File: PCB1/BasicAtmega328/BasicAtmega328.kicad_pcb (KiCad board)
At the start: 2 copper layers, 0 parts

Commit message: Placa enrutada
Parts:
- added C1: 47uF, Capacitors_SMD:CP_Elec_6.3x5.7, F.Cu at (110.5, 97.8)
- added C2: 100nF, Capacitors_SMD:C_0805, F.Cu at (104.1, 78.7)
- added C3: 4.7uF, Capacitors_SMD:C_0805, F.Cu at (102.5, 77.1)
- added C5: 100nF, Capacitors_SMD:C_0805, F.Cu at (113.6, 89.5)
- added C6: 100nF, Capacitors_SMD:C_0805, F.Cu at (97.3, 97.6)
- added C7: 10uF, Capacitors_SMD:C_0805, F.Cu at (118.8, 82.0)
- added C8: 100nF, Capacitors_SMD:C_0805, F.Cu at (118.8, 80.1)
- added D1: MBRA140, Diodes_SMD:D_SMA_Standard, F.Cu at (121.5, 93.0)
- added D2: POWER_ON, LEDs:LED_0805, B.Cu at (113.0, 105.4)
- added D3: SMBJ6.0CA, Diode_SMD:D_SMB, B.Cu at (117.4, 71.3)
- added D4: SMBJ6.0CA, Diode_SMD:D_SMB, B.Cu at (109.1, 71.3)
- added D5: SMBJ6.0CA, Diode_SMD:D_SMB, B.Cu at (100.8, 71.3)
- added F1: 160mA, Fuses:1206, B.Cu at (123.4, 66.4)
- added F2: 160mA, Fuses:1206, B.Cu at (94.7, 66.3)
- added J1: Jack-DC-IN, Connectors:BARREL_JACK, F.Cu at (118.8, 97.0)
- added JP1: VCC_CUT, Jumpers:SMT-JUMPER_2_NO_NO-SILK, B.Cu at (97.5, 84.7)
- added JP2: VCC_CUT, Jumpers:SMT-JUMPER_2_NO_NO-SILK, B.Cu at (119.1, 80.4)
- added JP3: VCC_CUT, Jumpers:SMT-JUMPER_2_NO_NO-SILK, B.Cu at (100.6, 104.3)
- added P1: ISCP, Connectors:2X3, F.Cu at (94.9, 89.3)
- added P2: HEADER1, Pin_Headers:Pin_Header_Straight_1x15, F.Cu at (88.4, 64.2)
- added P3: MODBUS_1, Connectors_Molex:Molex_Microfit3_Header_02x03_Angled_43045-060x, F.Cu at (113.7, 63.4)
- added P4: SERIAL_DEBUG, Connectors_JST:JST_PH_S4B-PH-K_04x2.00mm_Angled, F.Cu at (102.5, 105.0)
- added P5: MODBUS_2, Connectors_Molex:Molex_Microfit3_Header_02x03_Angled_43045-060x, F.Cu at (97.9, 63.4)
- added P6: HEADER2, Pin_Headers:Pin_Header_Straight_1x15, F.Cu at (129.4, 64.4)
- added R1: 1k, Resistors_SMD:R_0805, B.Cu at (113.0, 103.5)
- added R2: 10k, Resistors_SMD:R_0805, F.Cu at (108.1, 74.0)
- added R3: 10k, Resistors_SMD:R_0805, F.Cu at (108.1, 75.9)
- added R4: 1k, Resistors_SMD:R_0805, F.Cu at (98.6, 104.6)
- added R5: 10k, Resistors_SMD:R_0805, F.Cu at (124.1, 73.9)
- added R6: 10k, Resistors_SMD:R_0805, F.Cu at (122.2, 69.8)
- added R7: 10k, Resistors_SMD:R_0805, F.Cu at (111.7, 75.4)
- added R8: 120R(NC), Resistors_SMD:R_0805, B.Cu at (115.3, 73.8)
- added SW1: RESET_Button, Buttons_Switches_SMD:SW_SPST_B3U-3000P, F.Cu at (95.0, 105.1)
- added U1: LM1117-5.0, TO_SOT_Packages_SMD:SOT-223-3_TabPin2, F.Cu at (102.6, 97.9)
- added U2: ATMEGA328P-AU, Housings_QFP:TQFP-32_7x7mm_Pitch0.8mm, F.Cu at (108.1, 84.8)
- added U3: MAX13487E, Housings_SOIC:SO-8_5.3x6.2mm_Pitch1.27mm, F.Cu at (117.9, 75.7)
- added Y1: 16Mhz, Clocks:RESONATOR-SMD-3.2X1.3, F.Cu at (101.2, 81.5)
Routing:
- net +5V: track 0.00 -> 131.6 mm, vias 0 -> 5
- net +12V: track 0.00 -> 102.0 mm, vias 0 -> 3
- net RST: track 0.00 -> 95.8 mm, vias 0 -> 5
- net TXD: track 0.00 -> 59.0 mm, vias 0 -> 2
- net RXD: track 0.00 -> 58.1 mm, vias 0 -> 3
- net 485_TX: track 0.00 -> 49.6 mm, vias 0 -> 3
- net D13-SCK: track 0.00 -> 49.0 mm, vias 0 -> 7
- net 485_RX: track 0.00 -> 41.1 mm, vias 0 -> 2
- net Net-(D4-Pad2): track 0.00 -> 32.3 mm, vias 0 -> 2
- net D12-MISO: track 0.00 -> 31.0 mm
- net D11-MOSI: track 0.00 -> 29.5 mm, vias 0 -> 1
- net Net-(D3-Pad2): track 0.00 -> 28.6 mm, vias 0 -> 3
- net A6: track 0.00 -> 26.0 mm, vias 0 -> 2
- net A7: track 0.00 -> 25.4 mm, vias 0 -> 2
- net D10: track 0.00 -> 25.0 mm
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- added copper zone on B.Cu, net GND
- added copper zone on F.Cu, net GND
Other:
- board outline added: 45 x 49.9 mm

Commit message: Serigrafia añadida, faltan logos y DRC
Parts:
- added REF**: MountingHole_3.2mm_M3, Mounting_Holes:MountingHole_3.2mm_M3, F.Cu at (87.9, 106.6)
- added REF**: MountingHole_3.2mm_M3, Mounting_Holes:MountingHole_3.2mm_M3, F.Cu at (129.8, 106.7)
- added REF**: MountingHole_3.2mm_M3, Mounting_Holes:MountingHole_3.2mm_M3, F.Cu at (129.8, 58.5)
- added REF**: MountingHole_3.2mm_M3, Mounting_Holes:MountingHole_3.2mm_M3, F.Cu at (87.9, 58.4)
- moved D2 3.86 mm to (112.0, 109.1)
- moved R1 3.86 mm to (112.1, 107.2)
- moved SW1 3.55 mm to (96.2, 108.4)
- moved JP3 3.08 mm to (97.6, 103.3)
- moved R4 2.39 mm to (96.4, 105.5), turned to 180 degrees
- moved R8 2.21 mm to (117.3, 74.9)
- moved P4 1.15 mm to (101.4, 104.9)
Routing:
- net +5V: track 131.6 -> 142.3 mm
- net GND: track 9.15 -> 13.9 mm, vias 55 -> 88
- net RST: track 95.8 -> 99.5 mm
- net RXD: track 58.1 -> 61.1 mm
- net Net-(D3-Pad2): track 28.6 -> 31.1 mm
- net Net-(JP3-Pad2): track 3.04 -> 5.19 mm
- net Net-(D4-Pad2): track 32.3 -> 30.6 mm
- net A2: track 17.8 -> 18.5 mm
- net D6: track 17.6 -> 17.0 mm
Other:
- board size 45 x 49.9 mm -> 48.8 x 55.1 mm
- board text added: "BasicAtmega V0.1"

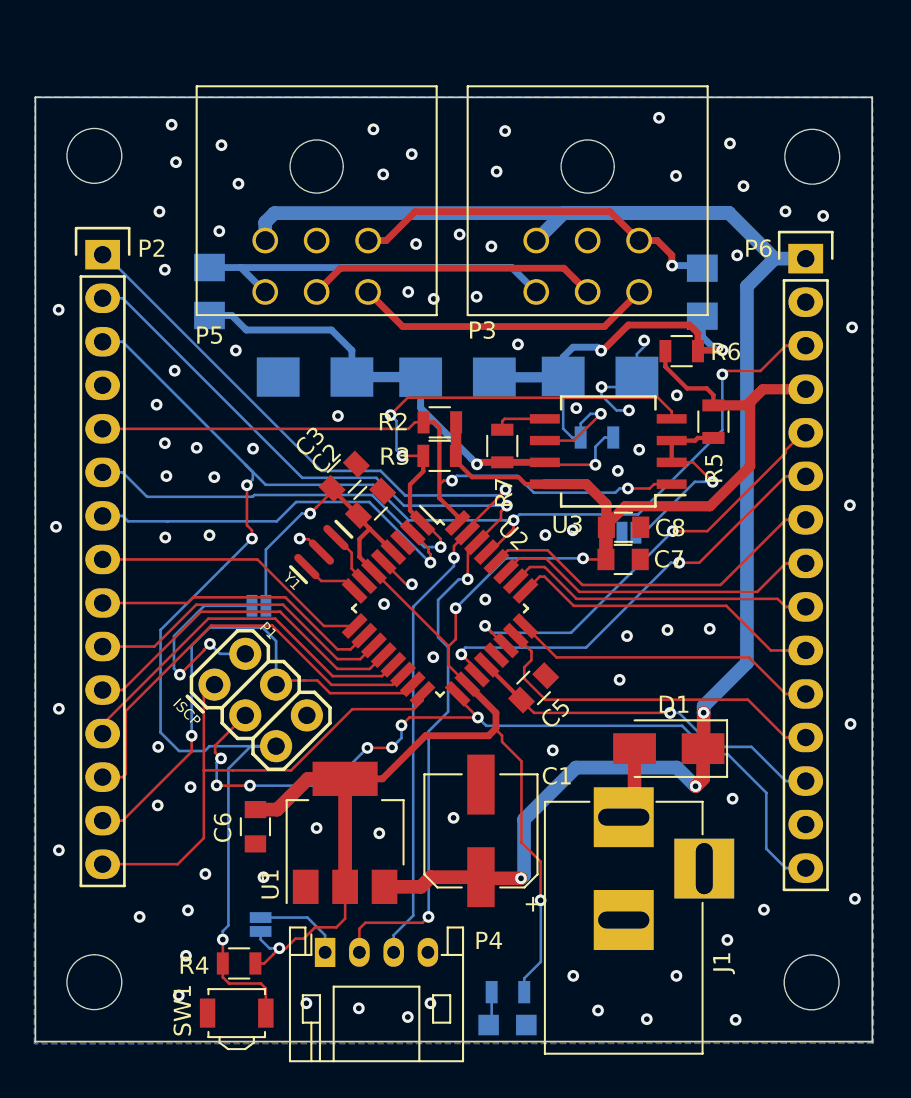
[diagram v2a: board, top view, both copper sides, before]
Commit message: Placas deconexion terminadas
Medidas exactas, esquema de drivers avanzado
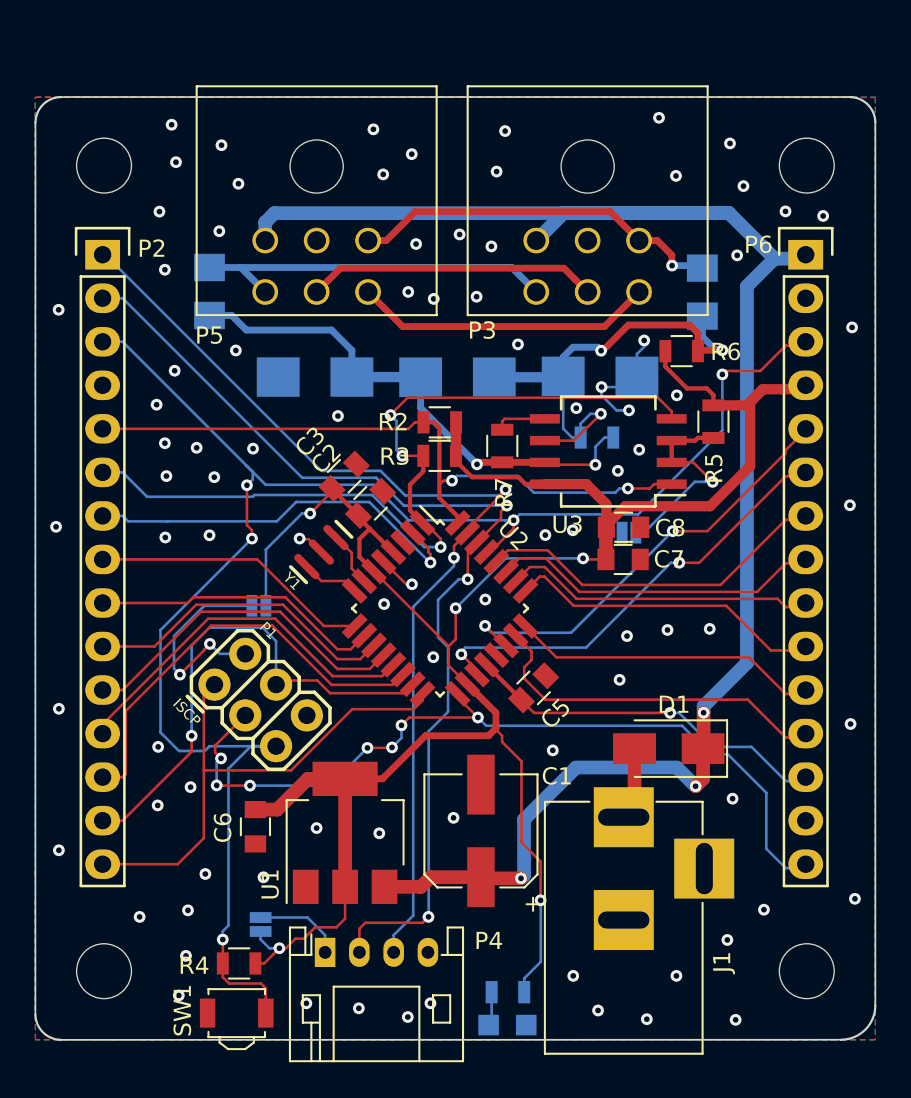
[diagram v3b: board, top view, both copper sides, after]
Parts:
- moved REF** 0.86 mm to (88.5, 106.0)
- moved REF** 0.80 mm to (88.5, 59.0)
- moved REF** 0.71 mm to (129.5, 106.0)
- moved REF** 0.61 mm to (129.5, 59.0)
- moved P6 0.23 mm to (129.4, 64.2)
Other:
- board size 48.8 x 55.1 mm -> 49 x 55 mm

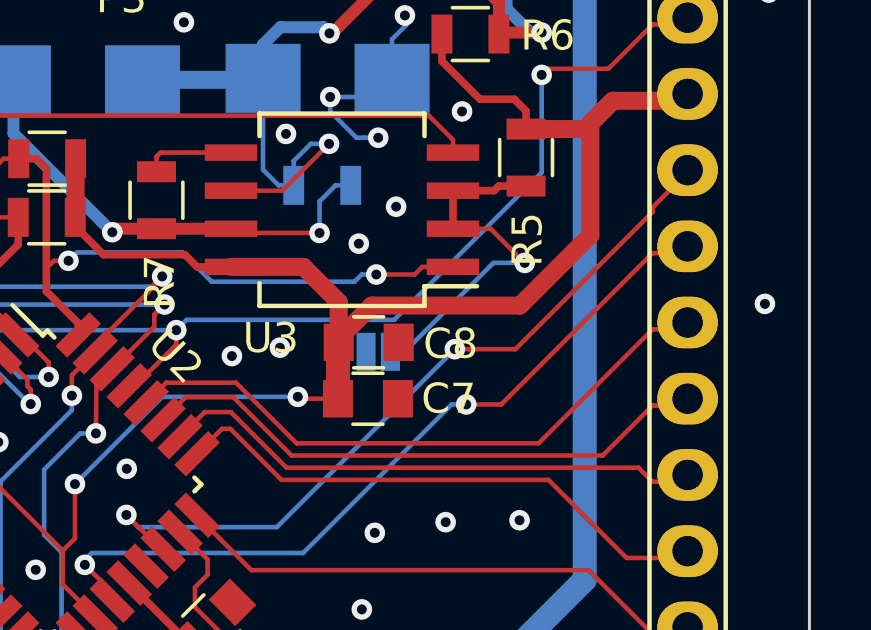
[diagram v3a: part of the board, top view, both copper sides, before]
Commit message: Placa driver casi enrutada, step y medidas exportadas
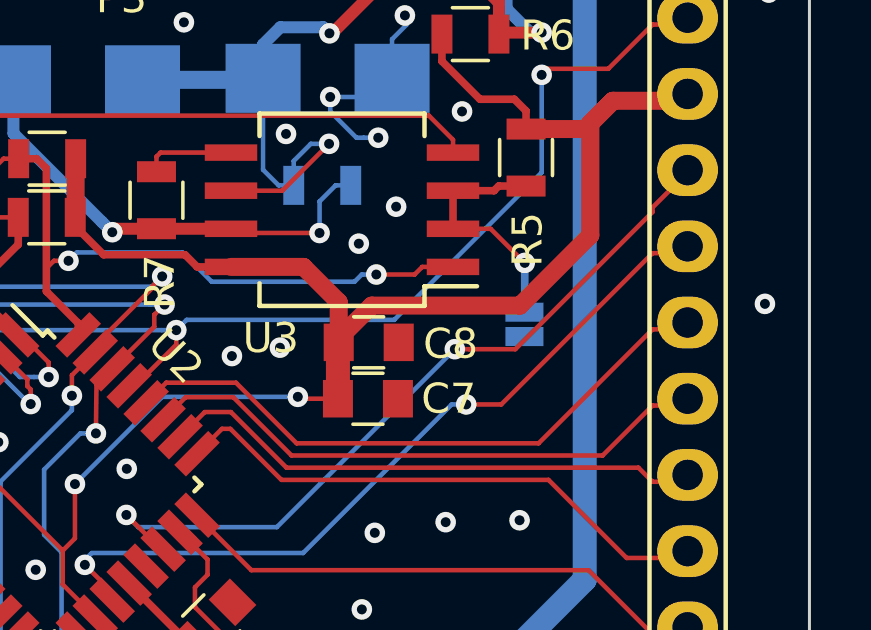
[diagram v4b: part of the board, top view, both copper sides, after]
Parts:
- added G***: LOGO, logos_frizzy:logoWTF_small, B.Cu at (107.0, 80.0)
- moved JP2 4.96 mm to (124.0, 79.5), turned to 90 degrees
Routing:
- net Net-(JP2-Pad2): track 12.3 -> 8.28 mm
